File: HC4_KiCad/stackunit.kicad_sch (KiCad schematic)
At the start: 18 parts, among them IC11 74HC161, IC12 74HC377

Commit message: ドキュメンテーションをちょっと充実
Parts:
- RN3: value R_Network04_Split -> 1k
- RN4: value R_Network08_Split -> 1k
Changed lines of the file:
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@@
 			)
 		)
-		(property "Value" "R_Network04_Split"
+		(property "Value" "1k"
 			(at 147.32 153.6701 0)
 			(effects
@@
 			)
 		)
-		(property "Value" "R_Network04_Split"
+		(property "Value" "1k"
 			(at 152.4 153.6701 0)
 			(effects
@@
 			)
 		)
-		(property "Value" "R_Network08_Split"
+		(property "Value" "1k"
 			(at 193.04 153.6701 0)
 			(effects
@@
 			)
 		)
-		(property "Value" "R_Network08_Split"
+		(property "Value" "1k"
 			(at 187.96 153.6701 0)
 			(effects
@@
 			)
 		)
-		(property "Value" "R_Network08_Split"
+		(property "Value" "1k"
 			(at 157.48 153.6701 0)
 			(effects
@@
 			)
 		)
-		(property "Value" "R_Network04_Split"
+		(property "Value" "1k"
 			(at 137.16 153.6701 0)
 			(effects
@@
 			)
 		)
-		(property "Value" "R_Network08_Split"
+		(property "Value" "1k"
 			(at 162.56 153.6701 0)
 			(effects
@@
 			)
 		)
-		(property "Value" "R_Network08_Split"
+		(property "Value" "1k"
 			(at 182.88 153.6701 0)
 			(effects
@@
 			)
 		)
-		(property "Value" "R_Network04_Split"
+		(property "Value" "1k"
 			(at 142.24 153.6701 0)
 			(effects
@@
 			)
 		)
-		(property "Value" "R_Network08_Split"
+		(property "Value" "1k"
 			(at 172.72 153.6701 0)
 			(effects
@@
 			)
 		)
-		(property "Value" "R_Network08_Split"
+		(property "Value" "1k"
 			(at 177.8 153.6701 0)
 			(effects
@@
 			)
 		)
-		(property "Value" "R_Network08_Split"
+		(property "Value" "1k"
 			(at 167.64 153.6701 0)
 			(effects

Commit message: 回路の改良　試験は明日やる
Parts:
- removed RN3: 1k, Resistor_THT:R_Array_SIP5, symbol Device:R_Network04_Split
- added unit 4 of RN3
- added unit 3 of RN3
- added unit 2 of RN3
- added unit 1 of RN3
- renumbered RN4 to RN3
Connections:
- net GND: now also RN3.1 (R1), RN3.1 (R1), RN3.1 (R1), RN3.1 (R1)
- net at LD10.1 (K): now also RN3.3 (R2.2)
- net at LD11.1 (K): now also RN3.2 (R1.2)
- net at LD8.1 (K): now also RN3.5 (R4.2)
- net at LD9.1 (K): now also RN3.4 (R3.2)

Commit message: フットプリントをSOPに変更
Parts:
- CP10, CP11: footprint Capacitor_THT:C_Disc_D3.0mm_W1.6mm_P2.50mm -> Capacitor_SMD:C_0603_1608Metric
- IC11: footprint Package_DIP:DIP-16_W7.62mm_Socket -> Package_SO:SO-16_5.3x10.2mm_P1.27mm
- IC12: footprint Package_DIP:DIP-20_W7.62mm_Socket -> Package_SO:SOP-20_7.5x12.8mm_P1.27mm
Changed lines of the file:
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@@
 			)
 		)
-		(property "Footprint" "Package_DIP:DIP-20_W7.62mm_Socket"
+		(property "Footprint" "Package_SO:SOP-20_7.5x12.8mm_P1.27mm"
 			(at 167.64 101.6 0)
 			(effects
@@
 			)
 		)
-		(property "Footprint" "Capacitor_THT:C_Disc_D3.0mm_W1.6mm_P2.50mm"
+		(property "Footprint" "Capacitor_SMD:C_0603_1608Metric"
 			(at 98.7552 153.67 0)
 			(effects
@@
 			)
 		)
-		(property "Footprint" "Capacitor_THT:C_Disc_D3.0mm_W1.6mm_P2.50mm"
+		(property "Footprint" "Capacitor_SMD:C_0603_1608Metric"
 			(at 105.1052 153.67 0)
 			(effects
@@
 			)
 		)
-		(property "Footprint" "Package_DIP:DIP-16_W7.62mm_Socket"
+		(property "Footprint" "Package_SO:SO-16_5.3x10.2mm_P1.27mm"
 			(at 92.71 83.82 0)
 			(effects

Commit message: 基板ぬ
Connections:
- net at LD10.1 (K): now also RN3.4 (R3.2); no longer RN3.3 (R2.2)
- net at RN4.2 (R1.2): now also LD16.1 (K); no longer LD19.1 (K)
- net at RN4.3 (R2.2): now also LD17.1 (K); no longer LD18.1 (K)
- net at RN3.5 (R4.2): now also LD11.1 (K); no longer LD8.1 (K)
- net at RN3.9 (R8.2): now also LD15.1 (K); no longer LD12.1 (K)
- net at RN3.2 (R1.2): now also LD8.1 (K); no longer LD11.1 (K)
- net at RN4.4 (R3.2): now also LD18.1 (K); no longer LD17.1 (K)
- net at RN3.6 (R5.2): now also LD12.1 (K); no longer LD15.1 (K)
- net at RN4.5 (R4.2): now also LD19.1 (K); no longer LD16.1 (K)
- net at LD14.1 (K): now also RN3.8 (R7.2); no longer RN3.7 (R6.2)
- net at LD9.1 (K): now also RN3.3 (R2.2); no longer RN3.4 (R3.2)
- net at LD13.1 (K): now also RN3.7 (R6.2); no longer RN3.8 (R7.2)
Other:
- moved on the sheet: RN3A, RN3B, RN3C, RN3D, RN3E, RN3F, RN3G, RN3H, RN4A, RN4B, RN4C, RN4D

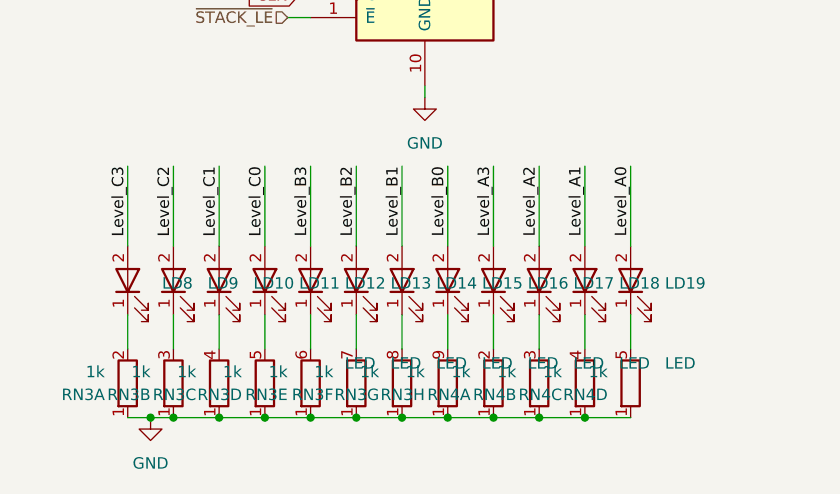
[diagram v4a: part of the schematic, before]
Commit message: Added output port for blink
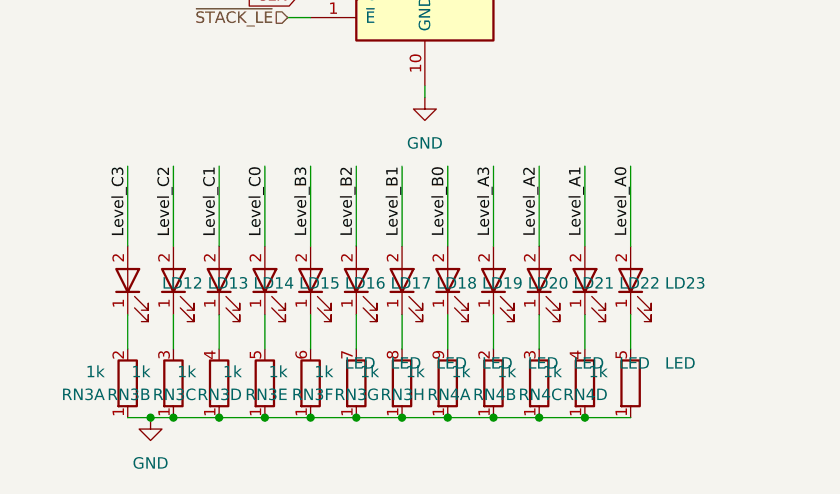
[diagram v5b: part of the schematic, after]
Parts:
- renumbered LD8 to LD12, LD9 to LD13, LD10 to LD14, LD11 to LD15, LD12 to LD16, LD13 to LD17, LD14 to LD18, LD15 to LD19, LD16 to LD20, LD17 to LD21, LD18 to LD22, LD19 to LD23
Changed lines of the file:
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@@
 		(on_board yes)
 		(dnp no)
-		(property "Reference" "LD10"
+		(property "Reference" "LD14"
 			(at 148.59 143.8274 90)
 			(effects
@@
 			)
 		)
-		(property "Datasheet" "~"
+		(property "Datasheet" ""
 			(at 144.78 143.51 0)
 			(effects
@@
 			(project "HC4_KiCad"
 				(path "/33731ded-38c0-4297-bdd8-92b082f46ff8/27e10803-908c-4418-a733-f902d25b5ad6"
-					(reference "LD10")
+					(reference "LD14")
 					(unit 1)
 				)
@@
 		(on_board yes)
 		(dnp no)
-		(property "Reference" "#PWR041"
+		(property "Reference" "#PWR040"
 			(at 167.64 81.28 0)
 			(effects
@@
 			(project ""
 				(path "/33731ded-38c0-4297-bdd8-92b082f46ff8/27e10803-908c-4418-a733-f902d25b5ad6"
-					(reference "#PWR041")
+					(reference "#PWR040")
 					(unit 1)
 				)
@@
 		(on_board yes)
 		(dnp no)
-		(property "Reference" "LD11"
+		(property "Reference" "LD15"
 			(at 153.67 143.8274 90)
 			(effects
@@
 			)
 		)
-		(property "Datasheet" "~"
+		(property "Datasheet" ""
 			(at 149.86 143.51 0)
 			(effects
@@
 			(project "HC4_KiCad"
 				(path "/33731ded-38c0-4297-bdd8-92b082f46ff8/27e10803-908c-4418-a733-f902d25b5ad6"
-					(reference "LD11")
+					(reference "LD15")
 					(unit 1)
 				)
@@
 		(on_board yes)
 		(dnp no)
-		(property "Reference" "LD17"
+		(property "Reference" "LD21"
 			(at 184.15 143.8274 90)
 			(effects
@@
 			)
 		)
-		(property "Datasheet" "~"
+		(property "Datasheet" ""
 			(at 180.34 143.51 0)
 			(effects
@@
 			(project "HC4_KiCad"
 				(path "/33731ded-38c0-4297-bdd8-92b082f46ff8/27e10803-908c-4418-a733-f902d25b5ad6"
-					(reference "LD17")
+					(reference "LD21")
 					(unit 1)
 				)
@@
 		(on_board yes)
 		(dnp no)
-		(property "Reference" "LD19"
+		(property "Reference" "LD23"
 			(at 194.31 143.8274 90)
 			(effects
@@
 			)
 		)
-		(property "Datasheet" "~"
+		(property "Datasheet" ""
 			(at 190.5 143.51 0)
 			(effects
@@
 			(project "HC4_KiCad"
 				(path "/33731ded-38c0-4297-bdd8-92b082f46ff8/27e10803-908c-4418-a733-f902d25b5ad6"
-					(reference "LD19")
+					(reference "LD23")
 					(unit 1)
 				)
@@
 		(dnp no)
 		(fields_autoplaced yes)
-		(property "Reference" "#PWR038"
+		(property "Reference" "#PWR037"
 			(at 100.33 149.86 0)
 			(effects
@@
 			(project ""
 				(path "/33731ded-38c0-4297-bdd8-92b082f46ff8/27e10803-908c-4418-a733-f902d25b5ad6"
-					(reference "#PWR038")
+					(reference "#PWR037")
 					(unit 1)
 				)
@@
 		(on_board yes)
 		(dnp no)
-		(property "Reference" "LD15"
+		(property "Reference" "LD19"
 			(at 173.99 143.8274 90)
 			(effects
@@
 			)
 		)
-		(property "Datasheet" "~"
+		(property "Datasheet" ""
 			(at 170.18 143.51 0)
 			(effects
@@
 			(project "HC4_KiCad"
 				(path "/33731ded-38c0-4297-bdd8-92b082f46ff8/27e10803-908c-4418-a733-f902d25b5ad6"
-					(reference "LD15")
+					(reference "LD19")
 					(unit 1)
 				)
@@
 		(on_board yes)
 		(dnp no)
-		(property "Reference" "#PWR040"
+		(property "Reference" "#PWR039"
 			(at 137.16 165.1 0)
 			(effects
@@
 			(project ""
 				(path "/33731ded-38c0-4297-bdd8-92b082f46ff8/27e10803-908c-4418-a733-f902d25b5ad6"
-					(reference "#PWR040")
+					(reference "#PWR039")
 					(unit 1)
 				)
@@
 		(on_board yes)
 		(dnp no)
-		(property "Reference" "LD8"
+		(property "Reference" "LD12"
 			(at 138.43 143.8274 90)
 			(effects
@@
 			)
 		)
-		(property "Datasheet" "~"
+		(property "Datasheet" ""
 			(at 134.62 143.51 0)
 			(effects
@@
 			(project "HC4_KiCad"
 				(path "/33731ded-38c0-4297-bdd8-92b082f46ff8/27e10803-908c-4418-a733-f902d25b5ad6"
-					(reference "LD8")
+					(reference "LD12")
 					(unit 1)
 				)
@@
 		(on_board yes)
 		(dnp no)
-		(property "Reference" "#PWR039"
+		(property "Reference" "#PWR038"
 			(at 100.33 160.02 0)
 			(effects
@@
 			(project ""
 				(path "/33731ded-38c0-4297-bdd8-92b082f46ff8/27e10803-908c-4418-a733-f902d25b5ad6"
-					(reference "#PWR039")
+					(reference "#PWR038")
 					(unit 1)
 				)
@@
 		(on_board yes)
 		(dnp no)
-		(property "Reference" "LD16"
+		(property "Reference" "LD20"
 			(at 179.07 143.8274 90)
 			(effects
@@
 			)
 		)
-		(property "Datasheet" "~"
+		(property "Datasheet" ""
 			(at 175.26 143.51 0)
 			(effects
@@
 			(project "HC4_KiCad"
 				(path "/33731ded-38c0-4297-bdd8-92b082f46ff8/27e10803-908c-4418-a733-f902d25b5ad6"
-					(reference "LD16")
+					(reference "LD20")
 					(unit 1)
 				)
@@
 		(on_board yes)
 		(dnp no)
-		(property "Reference" "LD14"
+		(property "Reference" "LD18"
 			(at 168.91 143.8274 90)
 			(effects
@@
 			)
 		)
-		(property "Datasheet" "~"
+		(property "Datasheet" ""
 			(at 165.1 143.51 0)
 			(effects
@@
 			(project "HC4_KiCad"
 				(path "/33731ded-38c0-4297-bdd8-92b082f46ff8/27e10803-908c-4418-a733-f902d25b5ad6"
-					(reference "LD14")
+					(reference "LD18")
 					(unit 1)
 				)
@@
 		(on_board yes)
 		(dnp no)
-		(property "Reference" "LD12"
+		(property "Reference" "LD16"
 			(at 158.75 143.8274 90)
 			(effects
@@
 			)
 		)
-		(property "Datasheet" "~"
+		(property "Datasheet" ""
 			(at 154.94 143.51 0)
 			(effects
@@
 			(project "HC4_KiCad"
 				(path "/33731ded-38c0-4297-bdd8-92b082f46ff8/27e10803-908c-4418-a733-f902d25b5ad6"
-					(reference "LD12")
+					(reference "LD16")
 					(unit 1)
 				)
@@
 		(dnp no)
 		(fields_autoplaced yes)
-		(property "Reference" "#PWR042"
+		(property "Reference" "#PWR041"
 			(at 167.64 129.54 0)
 			(effects
@@
 			(project ""
 				(path "/33731ded-38c0-4297-bdd8-92b082f46ff8/27e10803-908c-4418-a733-f902d25b5ad6"
-					(reference "#PWR042")
+					(reference "#PWR041")
 					(unit 1)
 				)
@@
 		(on_board yes)
 		(dnp no)
-		(property "Reference" "LD9"
+		(property "Reference" "LD13"
 			(at 143.51 143.8274 90)
 			(effects
@@
 			)
 		)
-		(property "Datasheet" "~"
+		(property "Datasheet" ""
 			(at 139.7 143.51 0)
 			(effects
@@
 			(project "HC4_KiCad"
 				(path "/33731ded-38c0-4297-bdd8-92b082f46ff8/27e10803-908c-4418-a733-f902d25b5ad6"
-					(reference "LD9")
+					(reference "LD13")
 					(unit 1)
 				)
@@
 		(on_board yes)
 		(dnp no)
-		(property "Reference" "#PWR036"
+		(property "Reference" "#PWR035"
 			(at 92.71 85.09 0)
 			(effects
@@
 			(project "HC4_KiCad"
 				(path "/33731ded-38c0-4297-bdd8-92b082f46ff8/27e10803-908c-4418-a733-f902d25b5ad6"
-					(reference "#PWR036")
+					(reference "#PWR035")
 					(unit 1)
 				)
@@
 		(on_board yes)
 		(dnp no)
-		(property "Reference" "LD18"
+		(property "Reference" "LD22"
 			(at 189.23 143.8274 90)
 			(effects
@@
 			)
 		)
-		(property "Datasheet" "~"
+		(property "Datasheet" ""
 			(at 185.42 143.51 0)
 			(effects
@@
 			(project "HC4_KiCad"
 				(path "/33731ded-38c0-4297-bdd8-92b082f46ff8/27e10803-908c-4418-a733-f902d25b5ad6"
-					(reference "LD18")
+					(reference "LD22")
 					(unit 1)
 				)
@@
 		(on_board yes)
 		(dnp no)
-		(property "Reference" "LD13"
+		(property "Reference" "LD17"
 			(at 163.83 143.8274 90)
 			(effects
@@
 			)
 		)
-		(property "Datasheet" "~"
+		(property "Datasheet" ""
 			(at 160.02 143.51 0)
 			(effects
@@
 			(project "HC4_KiCad"
 				(path "/33731ded-38c0-4297-bdd8-92b082f46ff8/27e10803-908c-4418-a733-f902d25b5ad6"
-					(reference "LD13")
+					(reference "LD17")
 					(unit 1)
 				)
@@
 		(dnp no)
 		(fields_autoplaced yes)
-		(property "Reference" "#PWR037"
+		(property "Reference" "#PWR036"
 			(at 92.71 123.19 0)
 			(effects
@@
 			(project "HC4_KiCad"
 				(path "/33731ded-38c0-4297-bdd8-92b082f46ff8/27e10803-908c-4418-a733-f902d25b5ad6"
-					(reference "#PWR037")
+					(reference "#PWR036")
 					(unit 1)
 				)

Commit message: moti
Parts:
- IC10: renamed from IC11; footprint Package_SO:SO-16_5.3x10.2mm_P1.27mm -> Package_DIP:DIP-16_W7.62mm
- IC11: renamed from IC12; footprint Package_SO:SOP-20_7.5x12.8mm_P1.27mm -> Package_DIP:DIP-20_W7.62mm
- renumbered CP11 to CP10, CP10 to CP9
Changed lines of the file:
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@@
 		(on_board yes)
 		(dnp no)
-		(property "Reference" "#PWR040"
+		(property "Reference" "#PWR041"
 			(at 167.64 81.28 0)
 			(effects
@@
 			(project ""
 				(path "/33731ded-38c0-4297-bdd8-92b082f46ff8/27e10803-908c-4418-a733-f902d25b5ad6"
-					(reference "#PWR040")
+					(reference "#PWR041")
 					(unit 1)
 				)
@@
 		(dnp no)
 		(fields_autoplaced yes)
-		(property "Reference" "IC12"
+		(property "Reference" "IC11"
 			(at 169.8341 81.28 0)
 			(effects
@@
 			)
 		)
-		(property "Footprint" "Package_SO:SOP-20_7.5x12.8mm_P1.27mm"
+		(property "Footprint" "Package_DIP:DIP-20_W7.62mm"
 			(at 167.64 101.6 0)
 			(effects
@@
 			(project ""
 				(path "/33731ded-38c0-4297-bdd8-92b082f46ff8/27e10803-908c-4418-a733-f902d25b5ad6"
-					(reference "IC12")
+					(reference "IC11")
 					(unit 1)
 				)
@@
 		(dnp no)
 		(fields_autoplaced yes)
-		(property "Reference" "#PWR037"
+		(property "Reference" "#PWR038"
 			(at 100.33 149.86 0)
 			(effects
@@
 			(project ""
 				(path "/33731ded-38c0-4297-bdd8-92b082f46ff8/27e10803-908c-4418-a733-f902d25b5ad6"
-					(reference "#PWR037")
+					(reference "#PWR038")
 					(unit 1)
 				)
@@
 		(on_board yes)
 		(dnp no)
-		(property "Reference" "#PWR039"
+		(property "Reference" "#PWR040"
 			(at 137.16 165.1 0)
 			(effects
@@
 			(project ""
 				(path "/33731ded-38c0-4297-bdd8-92b082f46ff8/27e10803-908c-4418-a733-f902d25b5ad6"
-					(reference "#PWR039")
+					(reference "#PWR040")
 					(unit 1)
 				)
@@
 		(on_board yes)
 		(dnp no)
-		(property "Reference" "#PWR038"
+		(property "Reference" "#PWR039"
 			(at 100.33 160.02 0)
 			(effects
@@
 			(project ""
 				(path "/33731ded-38c0-4297-bdd8-92b082f46ff8/27e10803-908c-4418-a733-f902d25b5ad6"
-					(reference "#PWR038")
+					(reference "#PWR039")
 					(unit 1)
 				)
@@
 		(on_board yes)
 		(dnp no)
-		(property "Reference" "CP10"
+		(property "Reference" "CP9"
 			(at 95.758 160.782 0)
 			(effects
@@
 			(project "HC4_KiCad"
 				(path "/33731ded-38c0-4297-bdd8-92b082f46ff8/27e10803-908c-4418-a733-f902d25b5ad6"
-					(reference "CP10")
+					(reference "CP9")
 					(unit 1)
 				)
@@
 		(on_board yes)
 		(dnp no)
-		(property "Reference" "CP11"
+		(property "Reference" "CP10"
 			(at 102.108 160.782 0)
 			(effects
@@
 			(project "HC4_KiCad"
 				(path "/33731ded-38c0-4297-bdd8-92b082f46ff8/27e10803-908c-4418-a733-f902d25b5ad6"
-					(reference "CP11")
+					(reference "CP10")
 					(unit 1)
 				)
@@
 		(dnp no)
 		(fields_autoplaced yes)
-		(property "Reference" "#PWR041"
+		(property "Reference" "#PWR042"
 			(at 167.64 129.54 0)
 			(effects
@@
 			(project ""
 				(path "/33731ded-38c0-4297-bdd8-92b082f46ff8/27e10803-908c-4418-a733-f902d25b5ad6"
-					(reference "#PWR041")
+					(reference "#PWR042")
 					(unit 1)
 				)
@@
 		(on_board yes)
 		(dnp no)
-		(property "Reference" "IC11"
+		(property "Reference" "IC10"
 			(at 95.504 81.534 0)
 			(effects
@@
 			)
 		)
-		(property "Footprint" "Package_SO:SO-16_5.3x10.2mm_P1.27mm"
+		(property "Footprint" "Package_DIP:DIP-16_W7.62mm"
 			(at 92.71 83.82 0)
 			(effects
@@
 			(project ""
 				(path "/33731ded-38c0-4297-bdd8-92b082f46ff8/27e10803-908c-4418-a733-f902d25b5ad6"
-					(reference "IC11")
+					(reference "IC10")
 					(unit 1)
 				)
@@
 		(on_board yes)
 		(dnp no)
-		(property "Reference" "#PWR035"
+		(property "Reference" "#PWR036"
 			(at 92.71 85.09 0)
 			(effects
@@
 			(project "HC4_KiCad"
 				(path "/33731ded-38c0-4297-bdd8-92b082f46ff8/27e10803-908c-4418-a733-f902d25b5ad6"
-					(reference "#PWR035")
+					(reference "#PWR036")
 					(unit 1)
 				)
@@
 		(dnp no)
 		(fields_autoplaced yes)
-		(property "Reference" "#PWR036"
+		(property "Reference" "#PWR037"
 			(at 92.71 123.19 0)
 			(effects
@@
 			(project "HC4_KiCad"
 				(path "/33731ded-38c0-4297-bdd8-92b082f46ff8/27e10803-908c-4418-a733-f902d25b5ad6"
-					(reference "#PWR036")
-					(unit 1)
-				)
+					(reference "#PWR037")
+					(unit 1)
+				)
